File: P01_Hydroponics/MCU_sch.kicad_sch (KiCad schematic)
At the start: 43 parts, among them J1 Conn_ST_STDC14, U1 STM32U545RETxQ, Y1 ASEK-32.768KHz-LRT, Y2 815-ASE-32.000MHZ-ET

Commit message: New version
Modified PD sink controller, and added 3v3 and 5V DC-DC buck converters
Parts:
- C1, C10, C13, C14, C2, C3, C4, C5, C6, C8: symbol Device:C -> Device:C_Small
- R1, R10, R11, R12, R13, R2, R3, R4, R5, R6, R7, R8, R9: symbol Device:R -> Device:R_Small
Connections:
- net GND: no longer C10.1
- net VUSB: no longer C10.2
- net VBAT renamed CMOS

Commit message: Need review
Please review the schematics.
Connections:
- net DM: now also TP2.1
- net DP: now also TP1.1
- net GND: now also C10.1
- net I2C_SCL: now also TP4.1
- net I2C_SDA: now also TP3.1
- net VUSB: now also C10.2
- net TEMP_DATA: now reaches U1.10 (PC2)
- net FLOW_DATA: now reaches U1.11 (PC3)
- net DIN: now reaches U1.16 (PA2)
- net ICH1: now reaches U1.37 (PC6)
- net ICH2: now reaches U1.38 (PC7)
- net LED_EN: now reaches U1.8 (PC0)
- net FLOW_EN: now reaches U1.9 (PC1)
- net PWM1 renamed PUMP_PWM
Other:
- moved on the sheet: R10, R11, R12, R13, R6, R7, R8, R9, TP1, TP10, TP2, TP3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

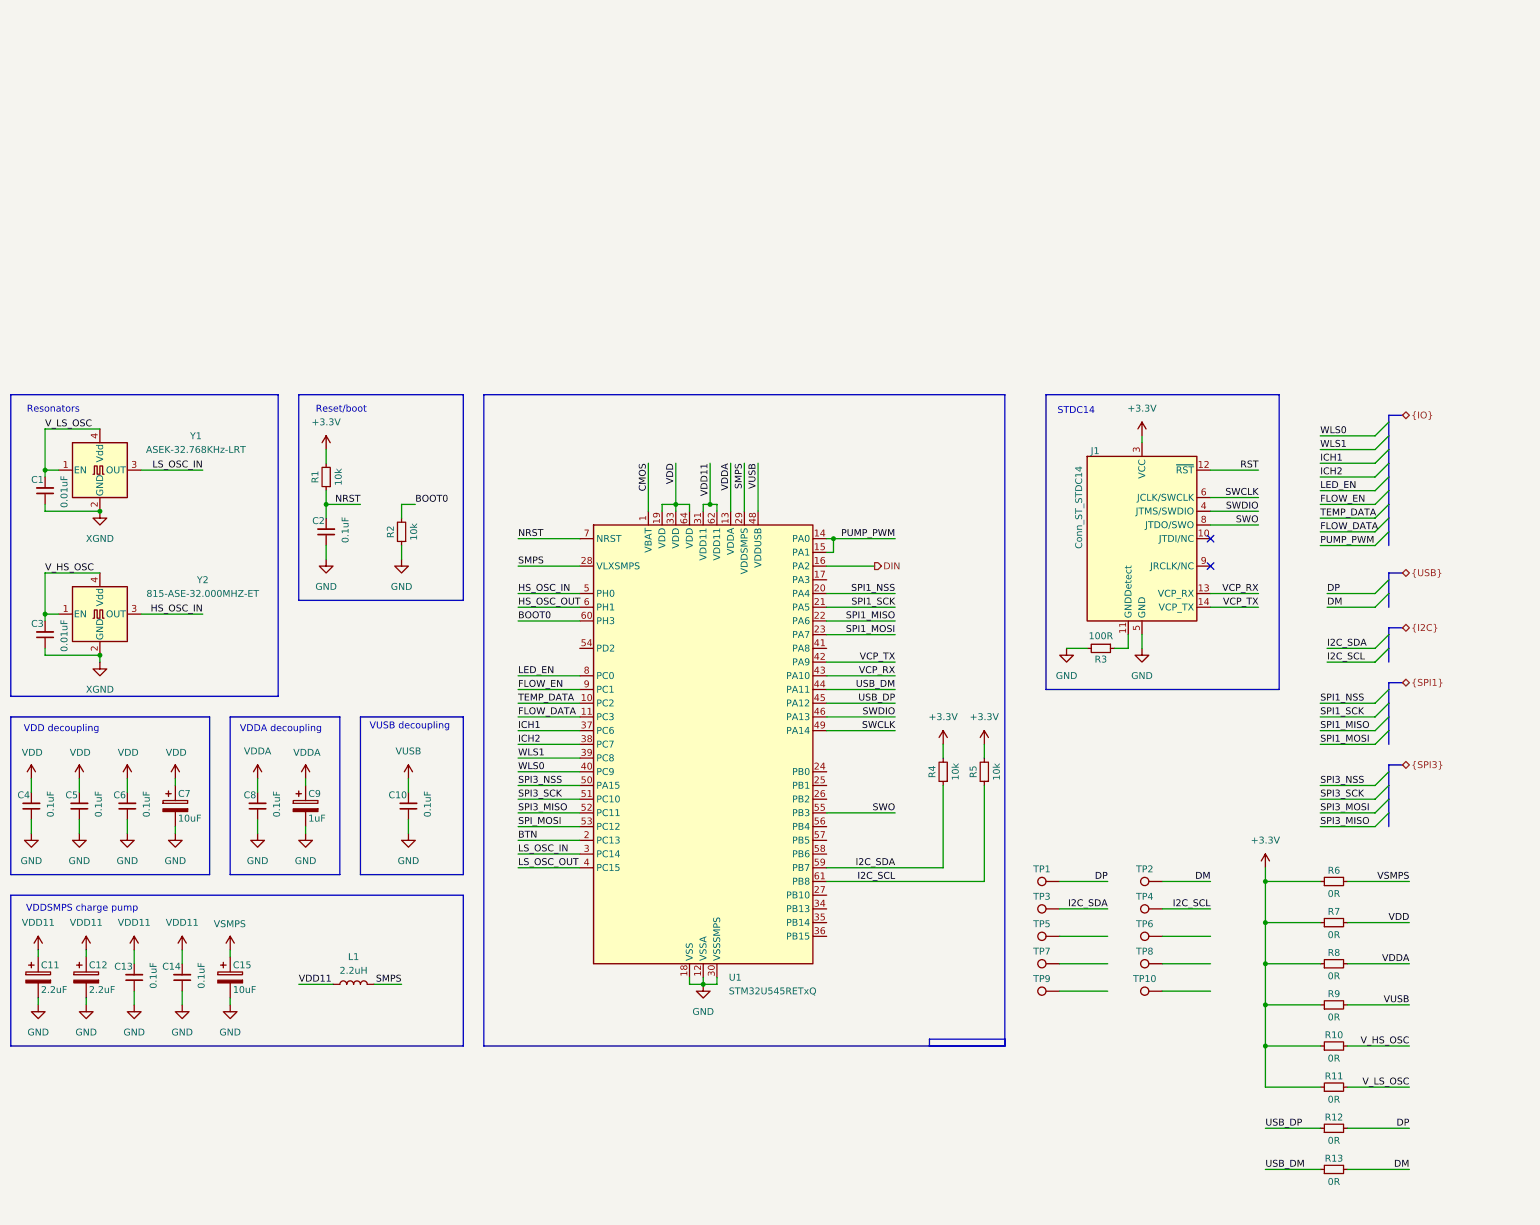
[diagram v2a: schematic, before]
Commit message: Need review
Updated:
STD14 to tag connect.
Added most footprints.
Change crystal to oscillator for ESP32
Rearrange radio controller schematic.
Added NOR flash.
Added USB-C connector for ESP32
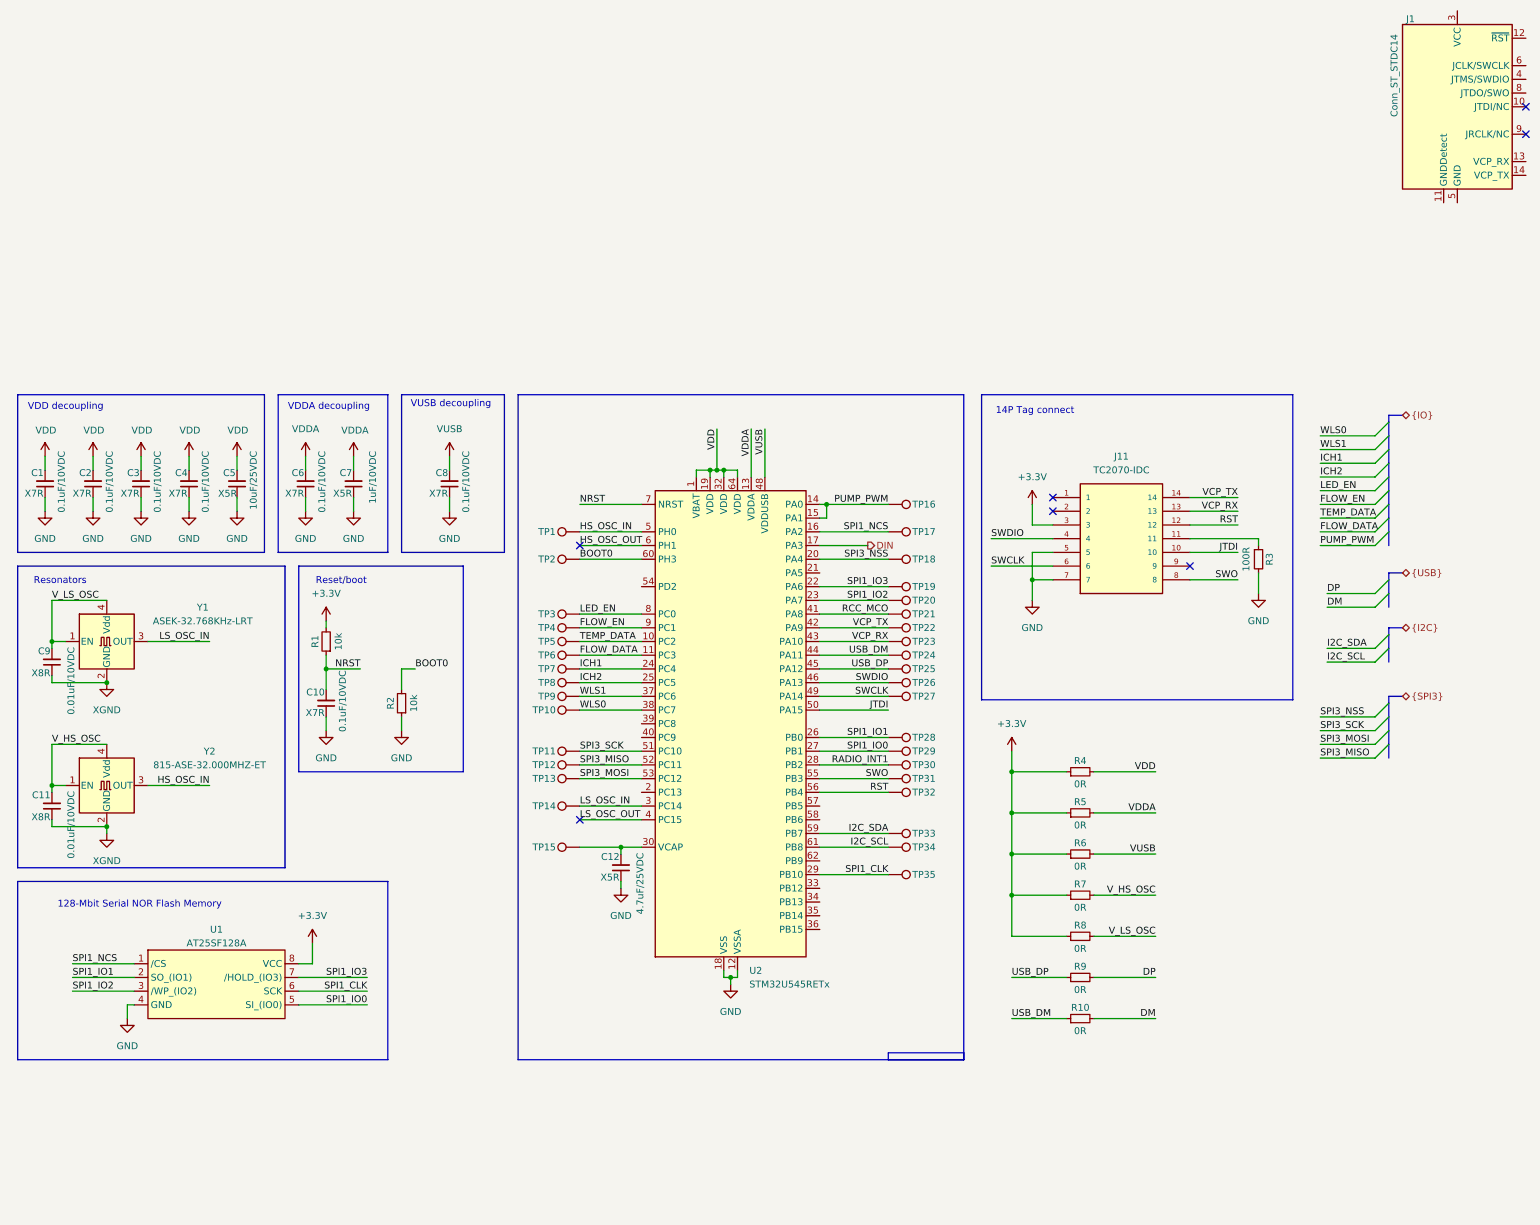
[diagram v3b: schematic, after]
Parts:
- removed C11, C12: 2.2uF, symbol Device:C_Polarized
- removed C13, C14: 0.1uF, symbol Device:C_Small
- removed C15, C7: 10uF, symbol Device:C_Polarized
- removed C9: 1uF, symbol Device:C_Polarized
- removed L1: 2.2uH, symbol Device:L
- removed R4, R5: 10k, symbol Device:R_Small
- removed R6: 0R, symbol Device:R_Small
- removed U1: STM32U545RETxQ, Package_QFP:LQFP-64_10x10mm_P0.5mm, symbol MCU_ST_STM32U5:STM32U545RETxQ
- added C1: 0.1uF/10VDC, Capacitor_SMD:C_0603_1608Metric_Pad1.08x0.95mm_HandSolder, symbol Device:C_Small
- added C11: 0.01uF/10VDC, Capacitor_SMD:C_0603_1608Metric_Pad1.08x0.95mm_HandSolder, symbol Device:C_Small
- added C12: 4.7uF/25VDC, Capacitor_SMD:C_0603_1608Metric_Pad1.08x0.95mm_HandSolder, symbol Device:C_Small
- added C7: 1uF/10VDC, Capacitor_SMD:C_0603_1608Metric_Pad1.08x0.95mm_HandSolder, symbol Device:C_Small
- added J11: TC2070-IDC, TC2070-IDC:TAG-CONNECT_TC2070-IDC, symbol TC2070-IDC:TC2070-IDC
- added TP11, TP12, TP13, TP14, TP15, TP16, TP17, TP18, TP19, TP20, TP21, TP22, TP23, TP24, TP25, TP26, TP27, TP28, TP29, TP30, TP31, TP32, TP33, TP34, TP35: ~, symbol Connector:TestPoint
- added U1: AT25SF128A, Package_SO:SOIC-8_7.5x5.85mm_P1.27mm, symbol QUAD_SPI_NOR_FLASH:AT25SF128A
- added U2: STM32U545RETx, Package_QFP:LQFP-64_10x10mm_P0.5mm, symbol MCU_ST_STM32U5:STM32U545RETx
- C10, C2, C4, C6, C8: value 0.1uF -> 0.1uF/10VDC; footprint (none) -> Capacitor_SMD:C_0603_1608Metric_Pad1.08x0.95mm_HandSolder; Dielectric (none) -> X7R
- C3: value 0.01uF -> 0.1uF/10VDC; footprint (none) -> Capacitor_SMD:C_0603_1608Metric_Pad1.08x0.95mm_HandSolder; Dielectric (none) -> X7R
- C5: value 0.1uF -> 10uF/25VDC; footprint (none) -> Capacitor_SMD:C_0603_1608Metric_Pad1.08x0.95mm_HandSolder; Dielectric (none) -> X5R
- C9: renamed from C1; value 0.01uF -> 0.01uF/10VDC; footprint (none) -> Capacitor_SMD:C_0603_1608Metric_Pad1.08x0.95mm_HandSolder; Dielectric (none) -> X8R
- R1, R2, R3: footprint (none) -> Resistor_SMD:R_0603_1608Metric_Pad0.98x0.95mm_HandSolder
- R10: renamed from R13; footprint (none) -> Resistor_SMD:R_0603_1608Metric_Pad0.98x0.95mm_HandSolder
- R4: renamed from R7; footprint (none) -> Resistor_SMD:R_0603_1608Metric_Pad0.98x0.95mm_HandSolder
- R5: renamed from R8; footprint (none) -> Resistor_SMD:R_0603_1608Metric_Pad0.98x0.95mm_HandSolder
- R6: renamed from R9; footprint (none) -> Resistor_SMD:R_0603_1608Metric_Pad0.98x0.95mm_HandSolder
- R7: renamed from R10; footprint (none) -> Resistor_SMD:R_0603_1608Metric_Pad0.98x0.95mm_HandSolder
- R8: renamed from R11; footprint (none) -> Resistor_SMD:R_0603_1608Metric_Pad0.98x0.95mm_HandSolder
- R9: renamed from R12; footprint (none) -> Resistor_SMD:R_0603_1608Metric_Pad0.98x0.95mm_HandSolder
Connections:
- net +3.3V: now also J11.3, U1.8 (VCC); no longer J1.3 (VCC)
- net BOOT0: now also TP2.1, U2.60 (PH3)
- net DIN: now also U2.17 (PA3)
- net DM: no longer TP2.1
- net DP: no longer TP1.1
- net FLOW_DATA: now also TP6.1, U2.11 (PC3)
- net FLOW_EN: now also TP4.1, U2.9 (PC1)
- net GND: now also C3.1, C1.1, C12.1, C7.1, J11.5, J11.7, U1.4 (GND), U2.12 (VSSA), U2.18 (VSS), U2.31 (VSS), U2.47 (VSS), U2.63 (VSS); no longer J1.5 (GND), J1.7 (GND)
- net HS_OSC_IN: now also TP1.1, U2.5 (PH0)
- net HS_OSC_OUT: now also U2.6 (PH1)
- net I2C_SCL: now also TP34.1, U2.61 (PB8); no longer TP4.1
- net I2C_SDA: now also TP33.1, U2.59 (PB7); no longer TP3.1
- net ICH1: now also TP7.1, U2.24 (PC4)
- net ICH2: now also TP8.1, U2.25 (PC5)
- net LED_EN: now also TP3.1, U2.8 (PC0)
- net LS_OSC_IN: now also TP14.1, U2.3 (PC14)
- net LS_OSC_OUT: now also U2.4 (PC15)
- net NRST: now also C10.2, U2.7 (NRST); no longer C2.2
- net PUMP_PWM: now also TP16.1, U2.14 (PA0), U2.15 (PA1)
- net RST: now also J11.12, TP32.1, U2.56 (PB4); no longer J1.12 (~{RST})
- net SPI3_MISO: now also TP12.1, U2.52 (PC11)
- net SPI3_MOSI: now also TP13.1, U2.53 (PC12)
- net SPI3_NSS: now also TP18.1, U2.20 (PA4)
- net SPI3_SCK: now also TP11.1, U2.51 (PC10)
- net SWCLK: now also J11.6, TP27.1, U2.49 (PA14); no longer J1.6 (JCLK/SWCLK)
- net SWDIO: now also J11.4, TP26.1, U2.46 (PA13); no longer J1.4 (JTMS/SWDIO)
- net SWO: now also J11.8, TP31.1, U2.55 (PB3); no longer J1.8 (JTDO/SWO)
- net TEMP_DATA: now also TP5.1, U2.10 (PC2)
- net USB_DM: now also TP24.1, U2.44 (PA11)
- net USB_DP: now also TP25.1, U2.45 (PA12)
- net VCP_RX: now also J11.13, TP23.1, U2.43 (PA10); no longer J1.13 (VCP_RX)
- net VCP_TX: now also J11.14, TP22.1, U2.42 (PA9); no longer J1.14 (VCP_TX)
- net VDD: now also C2.2, C3.2, C1.2, U2.1 (VBAT), U2.19 (VDD), U2.32 (VDD), U2.64 (VDD); no longer C6.2
- net VDDA: now also C6.2, C7.2, U2.13 (VDDA); no longer C8.2
- net VUSB: now also C8.2, U2.48 (VDDUSB); no longer C10.2
- net V_HS_OSC: now also C11.2; no longer C3.2
- net WLS0: now also TP10.1, U2.38 (PC7)
- net WLS1: now also TP9.1, U2.37 (PC6)
- net XGND: now also C11.1; no longer C3.1
- net at R3.1: now also J11.11; no longer J1.11 (GNDDetect)
- new net: C12.2, TP15.1, U2.30 (VCAP)
- new net: J1.5 (GND), J1.7 (GND)
- new net JTDI: J11.10, U2.50 (PA15)
- new net RADIO_INT1: TP30.1, U2.28 (PB2)
- new net RCC_MCO: TP21.1, U2.41 (PA8)
- new net SPI1_CLK: TP35.1, U1.6 (SCK), U2.29 (PB10)
- new net SPI1_IO0: TP29.1, U1.5 (SI_(IO0)), U2.27 (PB1)
- new net SPI1_IO1: TP28.1, U1.2 (SO_(IO1)), U2.26 (PB0)
- new net SPI1_IO2: TP20.1, U1.3 (/WP_(IO2)), U2.23 (PA7)
- new net SPI1_IO3: TP19.1, U1.7 (/HOLD_(IO3)), U2.22 (PA6)
- new net SPI1_NCS: TP17.1, U1.1 (/CS), U2.16 (PA2)
- no-connect marks 2 -> 7
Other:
- note added: "128-Mbit Serial NOR Flash Memory"
- note added: "14P Tag connect"
- note removed: "STDC14"
- note removed: "VDDSMPS charge pump"
- moved on the sheet: C9, J1, R1, R10, R2, R4, R5, R6, R7, R8, R9, Y1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
